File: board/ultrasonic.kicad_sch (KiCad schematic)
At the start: 17 parts, among them Q7 BSS123, T1 B78416A2232A003, U8 PGA460TPWR

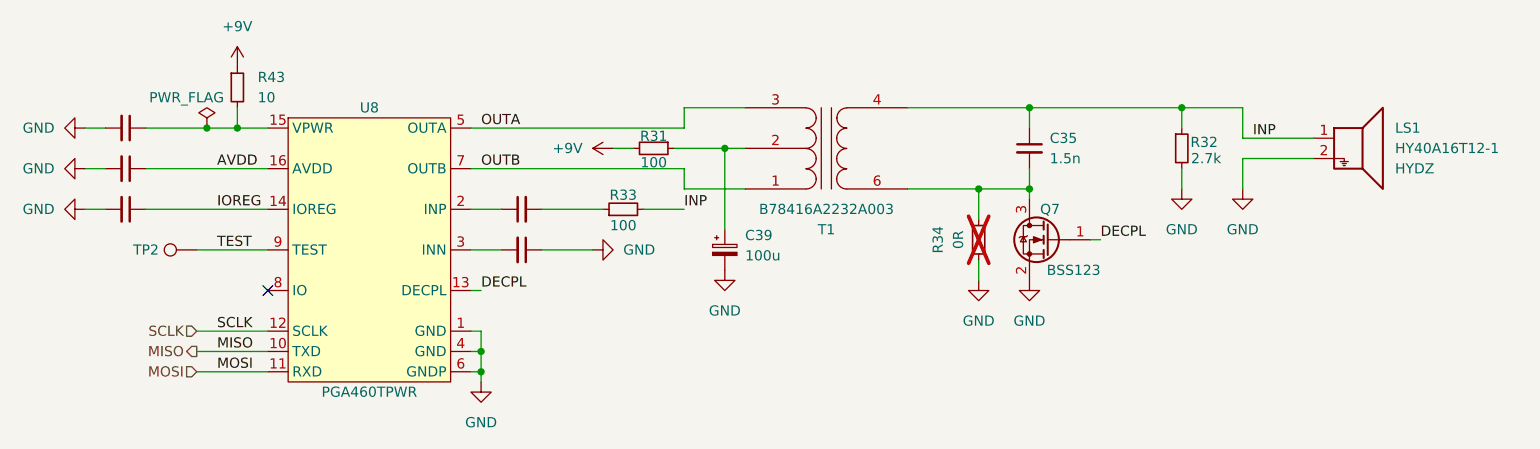
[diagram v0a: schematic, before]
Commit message: Update schematic and PCB layout
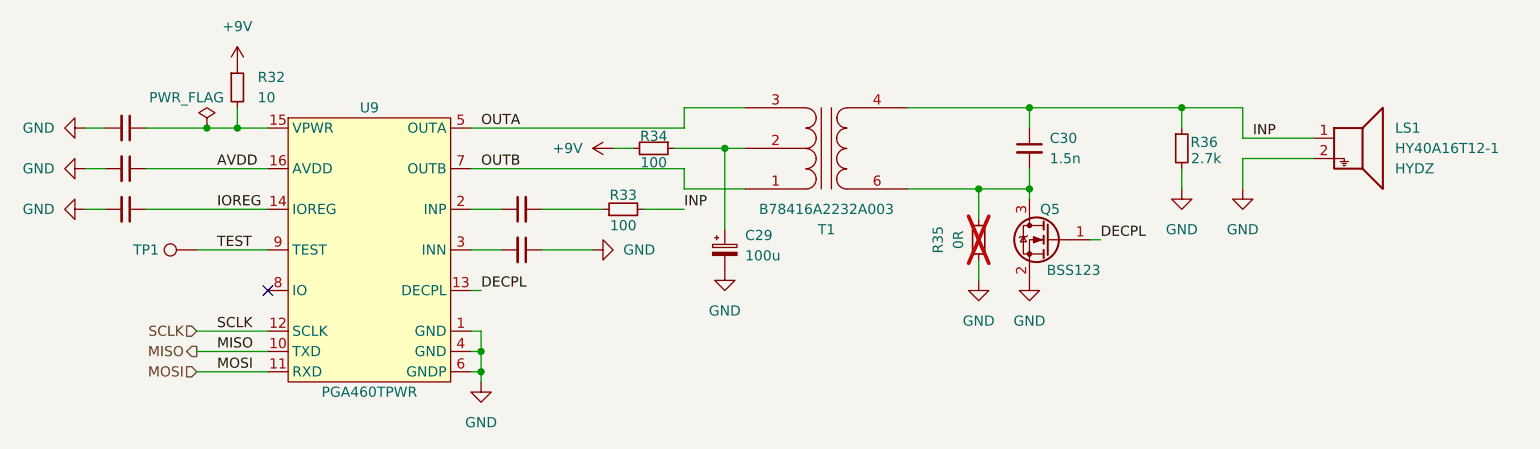
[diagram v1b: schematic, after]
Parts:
- renumbered C34 to C24, C36 to C25, C37 to C26, C38 to C27, C40 to C28, C39 to C29, C35 to C30, Q7 to Q5, R43 to R32, R31 to R34, R34 to R35, R32 to R36, TP2 to TP1, U8 to U9

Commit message: Various PCB tweaks, add power LED, add BOOT button
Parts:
- C24, C25, C26, C28: JLC_BasicPart yes -> (none); JLC_Price1 0.042 -> (none); JLC_Price10 0.0021 -> (none); JLC_Price100 0.0021 -> (none); JLC_Price1000 0.0014 -> (none); PCBA yes -> (none); kicost:JLC:pricing 1: USD 0.0020; 200: USD 0.0016; 800: USD 0.0013; 1600: USD 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 -> (none)
- C27, R33: JLC_BasicPart yes -> (none); PCBA yes -> (none)
- C29, C30, LS1, Q5, R32, T1, U9: JLC_BasicPart no -> (none)
- R34: JLC_BasicPart no -> (none); PCBA yes -> (none)
- R35: JLC_BasicPart yes -> (none); JLC_Price10 0.001 -> (none)
- R36: JLC_BasicPart yes -> (none)
